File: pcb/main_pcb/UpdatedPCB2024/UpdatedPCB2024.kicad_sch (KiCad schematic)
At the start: 29 parts

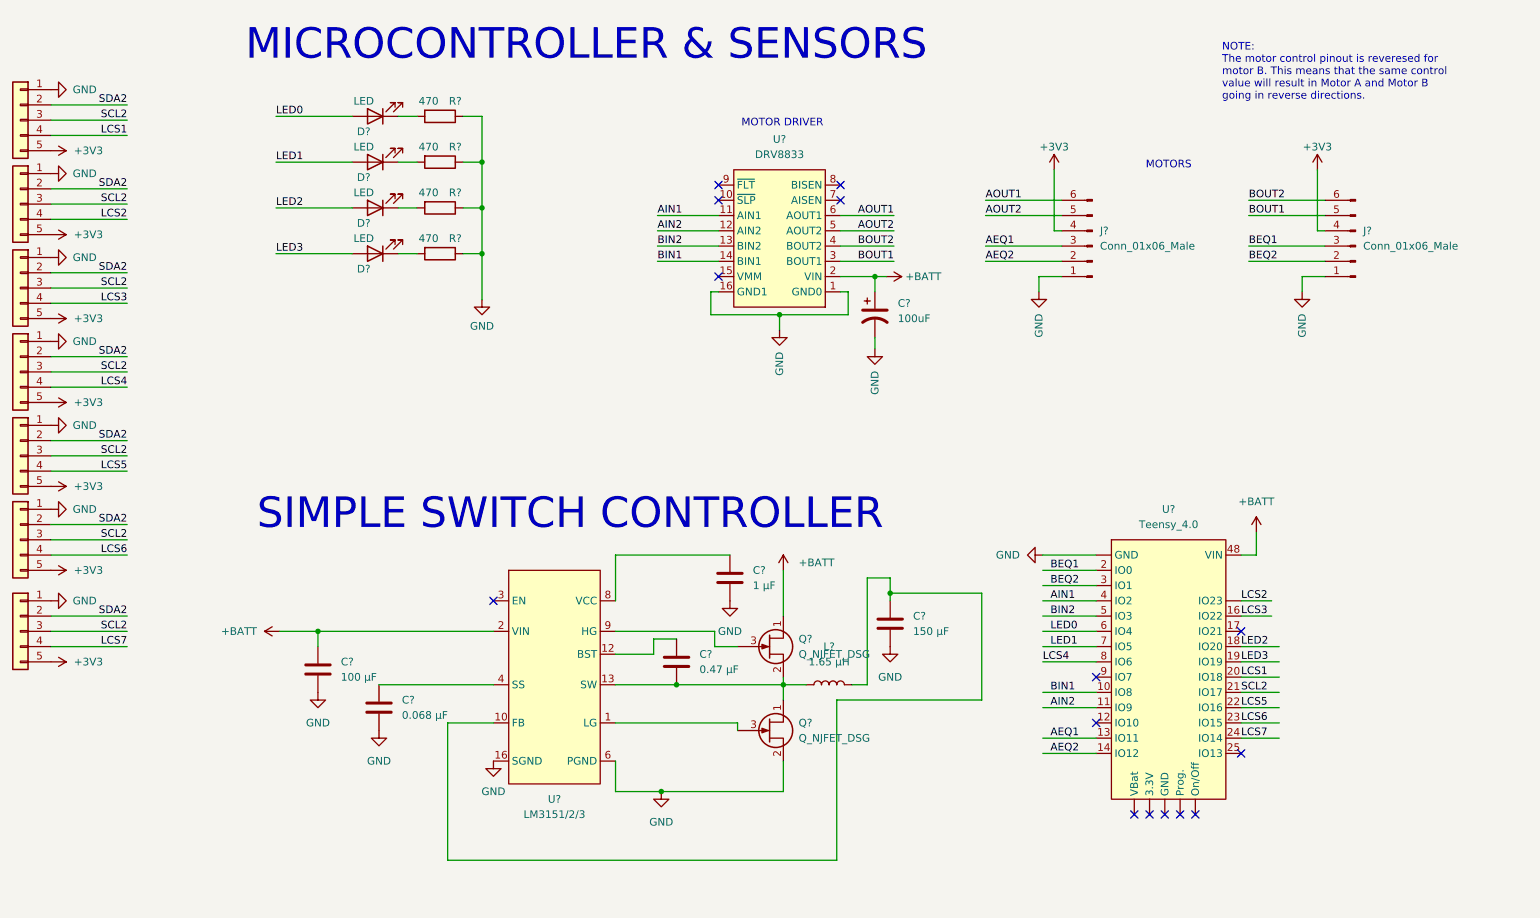
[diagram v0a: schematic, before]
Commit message: Footprint and labelling
Added the Teensy40 footprint into the custom-footprints.pretty folder, which will allow us to link the teensy40 footprint to the schematic we have. will still need to be readdressed.

Changed the raw text on the schematic to labels so that they will be recognized as connections rather than just text.
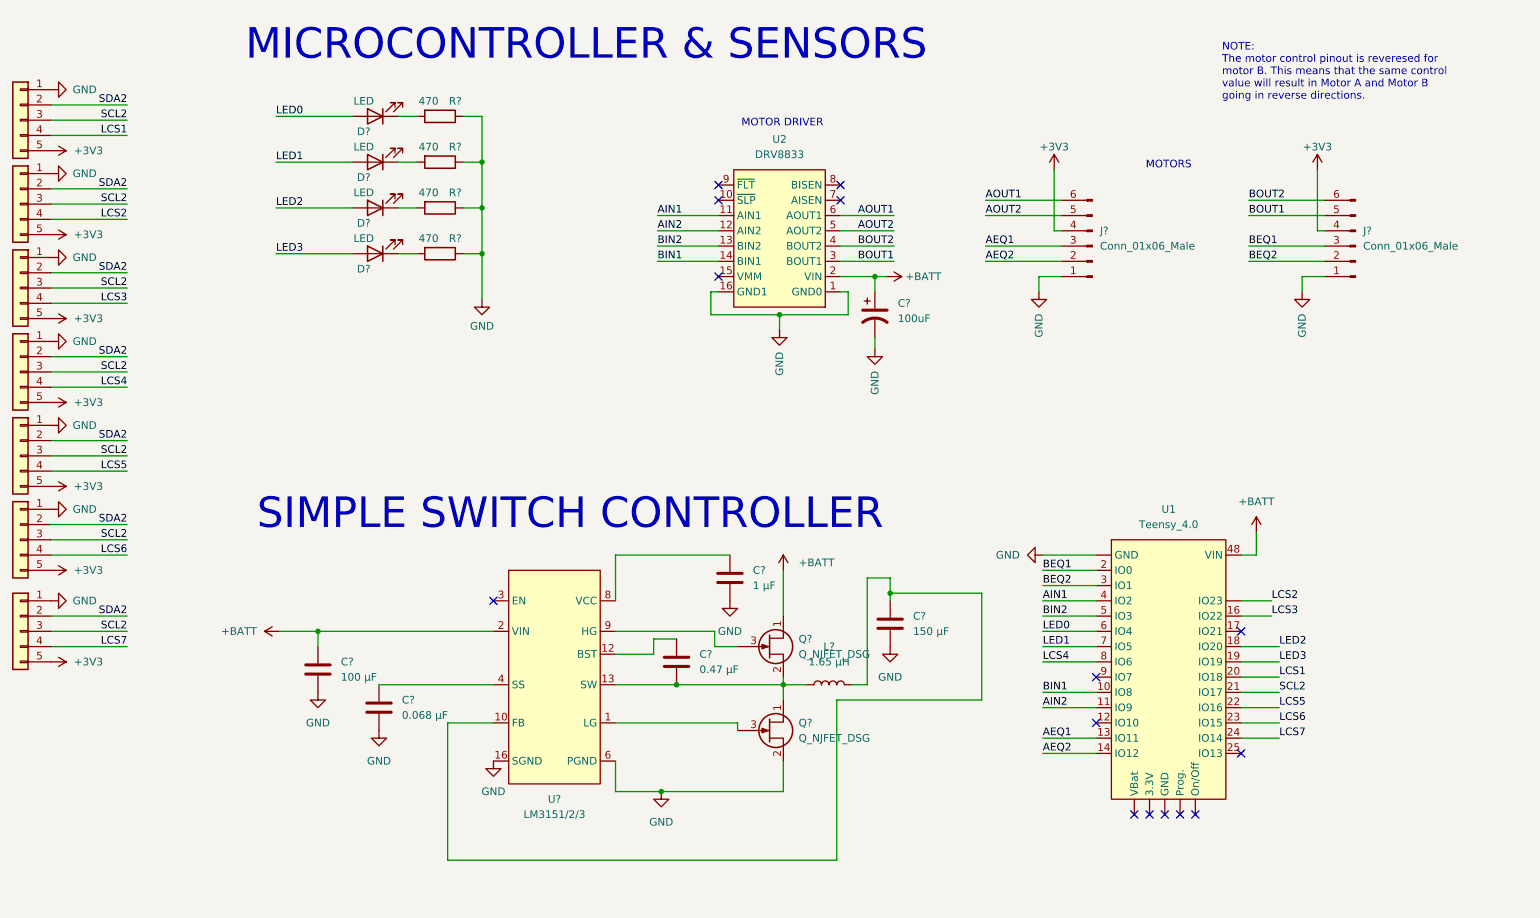
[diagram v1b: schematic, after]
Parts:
- gave numbers to parts that had none: 2

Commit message: Symbol footprint linking for teensy4
Changed some numbers and names around so that the footprint properly linked to the symbol for the Teensy4.0

We still need to assign footprints to the other circuit components that are not yet assigned, as well as update symbols as necessary.
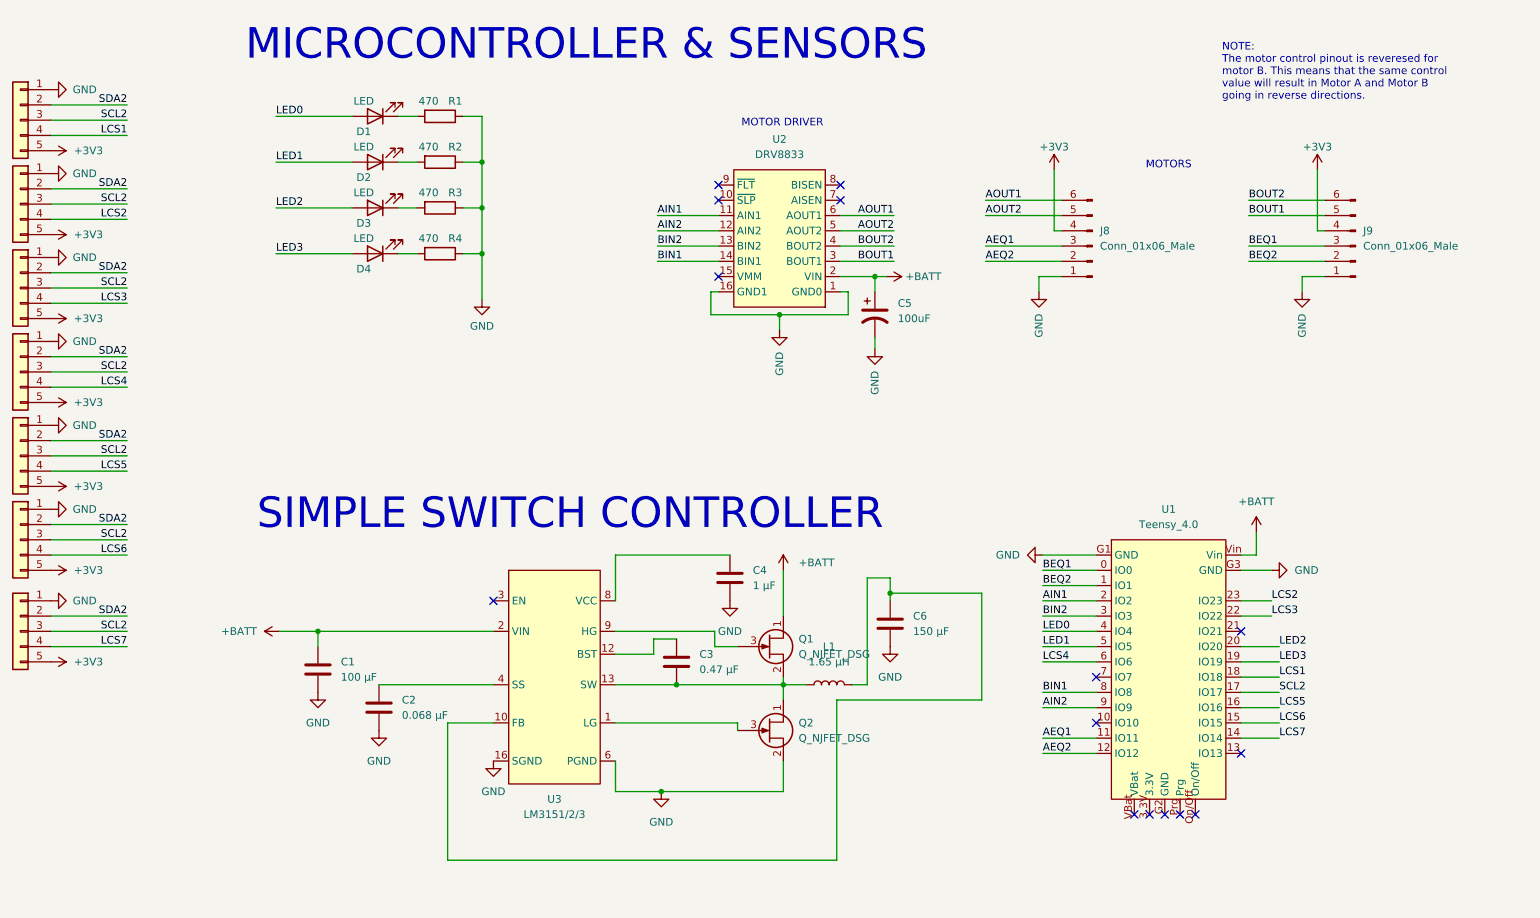
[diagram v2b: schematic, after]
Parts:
- U1: footprint (none) -> custom_footprints:Teensy40
- gave numbers to parts that had none: 27
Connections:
- net +BATT: now also U1.Vin; no longer U1.48 (VIN)
- net AEQ1: now also U1.11 (IO11); no longer U1.13 (IO11)
- net AEQ2: now also U1.12 (IO12); no longer U1.14 (IO12)
- net AIN1: now also U1.2 (IO2); no longer U1.4 (IO2)
- net AIN2: now also U1.9 (IO9); no longer U1.11 (IO9)
- net BEQ1: now also U1.0 (IO0); no longer U1.2 (IO0)
- net BEQ2: now also U1.1 (IO1); no longer U1.3 (IO1)
- net BIN1: now also U1.8 (IO8); no longer U1.10 (IO8)
- net BIN2: now also U1.3 (IO3); no longer U1.5 (IO3)
- net GND: now also U1.G1 (GND), U1.G3 (GND); no longer U1. (VBat)
- net LCS1: now also U1.18 (IO18); no longer U1.20 (IO18)
- net LCS2: now also U1.23 (IO23); no longer U1. (VBat)
- net LCS3: now also U1.22 (IO22); no longer U1.16 (IO22)
- net LCS4: now also U1.6 (IO6); no longer U1.8 (IO6)
- net LCS5: now also U1.16 (IO16); no longer U1.22 (IO16)
- net LCS6: now also U1.15 (IO15); no longer U1.23 (IO15)
- net LCS7: now also U1.14 (IO14); no longer U1.24 (IO14)
- net LED0: now also U1.4 (IO4); no longer U1.6 (IO4)
- net LED1: now also U1.5 (IO5); no longer U1.7 (IO5)
- net LED2: now also U1.20 (IO20); no longer U1.18 (IO20)
- net SCL2: now also U1.17 (IO17); no longer U1.21 (IO17)

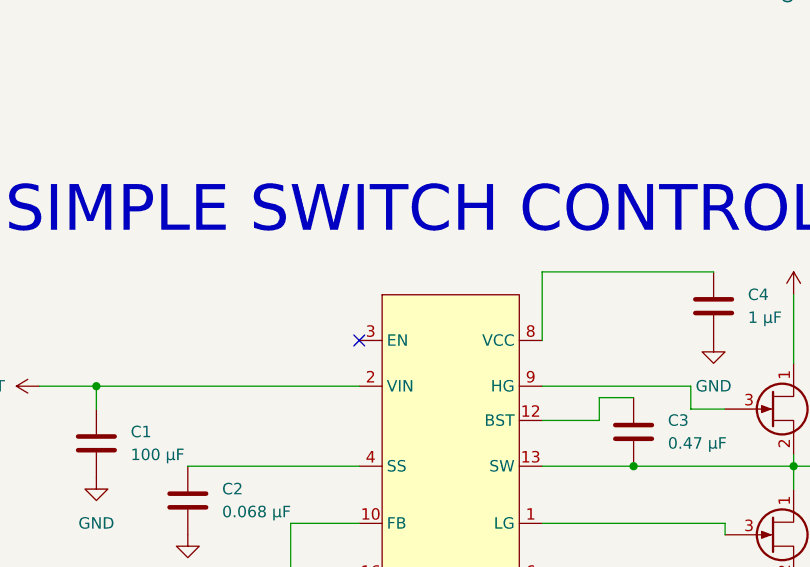
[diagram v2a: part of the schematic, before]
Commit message: adding footprints continued
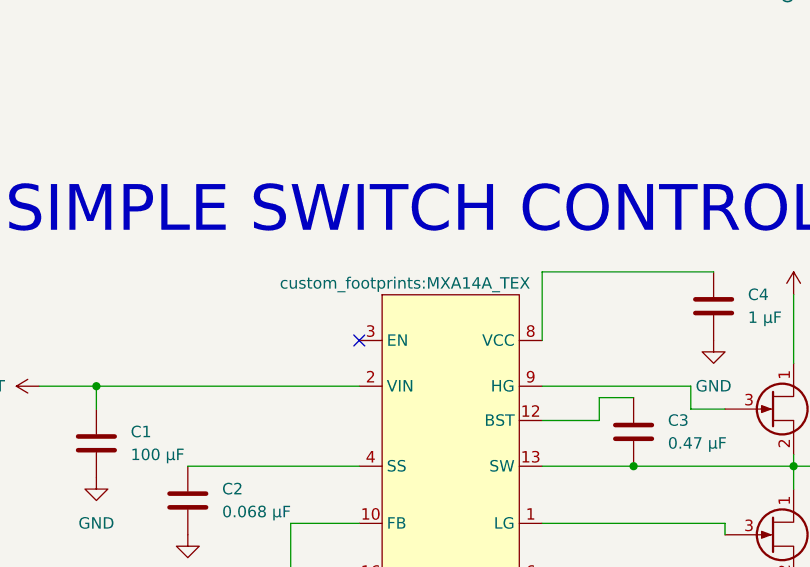
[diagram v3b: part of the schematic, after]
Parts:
- C1: footprint (none) -> custom_footprints:CHEMI-JA0
- C2: footprint (none) -> custom_footprints:0603_AVX
- C3: footprint (none) -> custom_footprints:CAP_2012_TDK
- C4: footprint (none) -> custom_footprints:CAPC220145_100N_KEM
- C6: footprint (none) -> custom_footprints:PCAP_EEF_SX_PAN
- Q1, Q2: footprint (none) -> custom_footprints:TRANS_RTR020N_ROM
- U3: footprint (none) -> custom_footprints:MXA14A_TEX
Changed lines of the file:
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@@
       (effects (font (size 1.27 1.27)) (justify left))
     )
-    (property "Footprint" "" (at 141.9352 115.57 0)
+    (property "Footprint" "custom_footprints:CAPC220145_100N_KEM" (at 141.9352 115.57 0)
       (effects (font (size 1.27 1.27)) hide)
     )
@@
       (effects (font (size 1.27 1.27)))
     )
-    (property "Footprint" "" (at 111.76 128.27 0)
+    (property "Footprint" "custom_footprints:MXA14A_TEX" (at 106.68 109.22 0)
       (effects (font (size 1.27 1.27)))
     )
@@
       (effects (font (size 1.27 1.27)) (justify left))
     )
-    (property "Footprint" "" (at 168.6052 123.19 0)
+    (property "Footprint" "custom_footprints:PCAP_EEF_SX_PAN" (at 168.6052 123.19 0)
       (effects (font (size 1.27 1.27)) hide)
     )
@@
       (effects (font (size 1.27 1.27)) (justify left))
     )
-    (property "Footprint" "" (at 152.4 134.62 0)
+    (property "Footprint" "custom_footprints:TRANS_RTR020N_ROM" (at 152.4 134.62 0)
       (effects (font (size 1.27 1.27)) hide)
     )
@@
       (effects (font (size 1.27 1.27)) (justify left))
     )
-    (property "Footprint" "" (at 152.4 120.65 0)
+    (property "Footprint" "custom_footprints:TRANS_RTR020N_ROM" (at 152.4 120.65 0)
       (effects (font (size 1.27 1.27)) hide)
     )
@@
       (effects (font (size 1.27 1.27)) (justify left))
     )
-    (property "Footprint" "" (at 83.5152 137.16 0)
+    (property "Footprint" "custom_footprints:0603_AVX" (at 83.5152 137.16 0)
       (effects (font (size 1.27 1.27)) hide)
     )
@@
       (effects (font (size 1.27 1.27)) (justify left))
     )
-    (property "Footprint" "" (at 73.3552 130.81 0)
+    (property "Footprint" "custom_footprints:CHEMI-JA0" (at 73.3552 130.81 0)
       (effects (font (size 1.27 1.27)) hide)
     )
@@
       (effects (font (size 1.27 1.27)) (justify left))
     )
-    (property "Footprint" "" (at 133.0452 129.54 0)
-      (effects (font (size 1.27 1.27)) hide)
-    )
+    (property "Footprint" "custom_footprints:CAP_2012_TDK" (at 133.0452 129.54 0)
+      (effects (font (size 1.27 1.27)) hide)
+    )

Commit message: Created L1 footprint
Created L1 footprint from product datasheet's recommended footprint.
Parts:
- L1: footprint (none) -> custom_footprints:HA3778-AL
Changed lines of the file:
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@@
       (effects (font (size 1.27 1.27)))
     )
-    (property "Footprint" "" (at 157.48 129.54 0)
+    (property "Footprint" "custom_footprints:HA3778-AL" (at 157.48 129.54 0)
       (effects (font (size 1.27 1.27)) hide)
     )
@@
     (pin "3.3V")
     (pin "4")
-    (pin "Vin")
     (pin "5")
     (pin "6")
@@
     (pin "Prg")
     (pin "VBat")
-    (instances
-      (project "UpdatedPCB2024"
+    (pin "Vin")
+    (instances
+      (project "UpdatedPCB2024"
